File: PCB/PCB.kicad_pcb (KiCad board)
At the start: 2 copper layers, 22 parts, among them J1 12V_IN, J10 Retorno_1, J11 Modulo_Relays, J12 Motor, J13 Retorno_2, J2 5V_OUT, J3 DHT11, J4 Buzzer, J5 Tx, J6 Humidificador, J7 Cooler, J8 Nucleo, J9 9V_OUT, U1 LM7805_TO220, U2 LM7809_TO220

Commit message: Actualizacion de PCB y esquematico
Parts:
- added C7: 10uF, Capacitor_THT:CP_Radial_D4.0mm_P2.00mm, F.Cu at (116.5, 70.0)
- added C8: 0.1uF, Capacitor_THT:C_Disc_D3.0mm_W1.6mm_P2.50mm, F.Cu at (116.2, 74.0)
- added H1: MountingHole_4.3mm_M4_ISO14580_Pad_TopBottom, MountingHole:MountingHole_4.3mm_M4_ISO14580_Pad_TopBottom, F.Cu at (67.5, 60.0)
- added H2: MountingHole_4.3mm_M4_ISO14580_Pad_TopBottom, MountingHole:MountingHole_4.3mm_M4_ISO14580_Pad_TopBottom, F.Cu at (67.5, 99.0)
- added H2: MountingHole_4.3mm_M4_ISO14580_Pad_TopBottom, MountingHole:MountingHole_4.3mm_M4_ISO14580_Pad_TopBottom, F.Cu at (129.7, 99.0)
- added H2: MountingHole_4.3mm_M4_ISO14580_Pad_TopBottom, MountingHole:MountingHole_4.3mm_M4_ISO14580_Pad_TopBottom, F.Cu at (129.7, 60.9)
- added J14: 3_3V_OUT, TerminalBlock_Phoenix:TerminalBlock_Phoenix_MKDS-1,5-2-5.08_1x02_P5.08mm_Horizontal, F.Cu at (115.0, 61.7)
- added U3: LD1117V33, Package_TO_SOT_THT:TO-220-3_Vertical, F.Cu at (116.0, 80.0)
- J5: footprint Connector_Molex:Molex_KK-254_AE-6410-02A_1x02_P2.54mm_Vertical -> Connector_Molex:Molex_KK-254_AE-6410-03A_1x03_P2.54mm_Vertical
- J8: footprint Connector_Molex:Molex_KK-254_AE-6410-08A_1x08_P2.54mm_Vertical -> Connector_Molex:Molex_KK-254_AE-6410-09A_1x09_P2.54mm_Vertical
- moved J13 85.9 mm to (129.0, 89.0), turned to 90 degrees
- moved J3 84.4 mm to (95.5, 100.5), turned to 180 degrees
- moved J10 75.5 mm to (115.0, 98.7), turned to 0 degrees
- moved J6 73.7 mm to (109.3, 100.5), turned to 180 degrees
- moved J8 73.1 mm to (66.5, 87.2), turned to 90 degrees
- moved J2 71.3 mm to (106.8, 61.2), turned to 180 degrees
- moved J1 69.4 mm to (92.0, 61.1), turned to 180 degrees
- moved U1 68.2 mm to (98.4, 78.5), turned to -90 degrees
- moved C3 67.8 mm to (105.2, 70.0), turned to 180 degrees
- moved J4 67.3 mm to (86.3, 100.5), turned to 180 degrees
- moved C4 65.7 mm to (105.5, 74.5), turned to 180 degrees
- moved C2 63.7 mm to (92.0, 75.3)
- moved C1 63.7 mm to (88.0, 75.5)
- moved J12 63.3 mm to (129.0, 77.5), turned to 90 degrees
- moved J7 62.1 mm to (102.3, 100.5), turned to 180 degrees
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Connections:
- J10 pad 2: unconnected-(J10-Pin_2-Pad2) -> B15_R
- J11 pad 2: +12V -> +5V
- J11 pad 6: +5V -> Pin_Motor
- J13 pad 1: +12V_R -> unconnected-(J13-Pin_1-Pad1)
- J13 pad 2: B15_R -> +12V_R
- J8 pad 1: PIN_LAMPARA -> A11
- J8 pad 2: B15 -> B12
- J8 pad 3: B13 -> A9
- J8 pad 4: A11 -> B15
- J8 pad 5: B12 -> B13
- J8 pad 6: A9 -> PIN_LAMPARA
- J8 pad 7: +9V -> Pin_Motor
- J8 pad 8: GND -> +9V
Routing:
- net GND: track 30.2 -> 288.4 mm
- net +3_3V: track 0.00 -> 135.4 mm
- net Net-(D1-K): track 0.00 -> 100.9 mm
- net +5V: track 0.00 -> 58.3 mm
- net A9: track 0.00 -> 35.0 mm
- net +9V: track 0.00 -> 34.6 mm
- net Pin_Motor: track 0.00 -> 31.3 mm
- net PIN_LAMPARA: track 0.00 -> 30.1 mm
- net B13: track 0.00 -> 29.3 mm
- net B15: track 0.00 -> 28.5 mm
- net B12: track 0.00 -> 27.3 mm
- net B15_R: track 0.00 -> 21.3 mm
- net A11: track 0.00 -> 20.3 mm
- net +12V_R: track 29.0 -> 10.8 mm
- net B13_R: track 0.00 -> 6.44 mm
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
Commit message: Actualizacion del PCB
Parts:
- added J15: Encoder_Rotativo, Connector_Molex:Molex_KK-254_AE-6410-05A_1x05_P2.54mm_Vertical, F.Cu at (155.5, 93.4)
- added J16: Encoder_Motor, Connector_Molex:Molex_KK-254_AE-6410-03A_1x03_P2.54mm_Vertical, F.Cu at (146.0, 96.0)
- added J17: LCD, Connector_Molex:Molex_KK-254_AE-6410-04A_1x04_P2.54mm_Vertical, F.Cu at (165.0, 102.3)
- J11: value Modulo_Relays -> Modulo_Reles
- J8: footprint Connector_Molex:Molex_KK-254_AE-6410-09A_1x09_P2.54mm_Vertical -> Connector_Molex:Molex_KK-254_AE-6410-15A_1x15_P2.54mm_Vertical
- moved J9 59.3 mm to (133.0, 73.2), turned to 180 degrees
- moved J14 56.3 mm to (170.0, 73.2), turned to 180 degrees
- moved J8 55.5 mm to (116.0, 112.4)
- moved D1 54.4 mm to (136.3, 82.0)
- moved J1 54.3 mm to (145.0, 73.2)
- moved C7 54.1 mm to (169.5, 80.9), turned to -90 degrees
- moved H4 53.7 mm to (179.5, 119.0)
- moved C3 53.6 mm to (157.5, 82.0)
- moved C4 53.6 mm to (157.8, 86.5)
- moved U3 53.1 mm to (168.5, 88.0)
- moved H3 52.9 mm to (116.5, 119.0)
- moved U1 51.9 mm to (150.2, 82.5)
- moved J2 51.7 mm to (157.0, 73.2)
- moved J4 51.5 mm to (135.2, 116.5)
- moved J6 51.5 mm to (158.2, 116.5)
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- renumbered H2 to H3, H2 to H4
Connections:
- J11 pad 3: B15 -> PIN_MOTOR
- J11 pad 4: B13 -> PIN_LAMPARA
- J11 pad 5: PIN_LAMPARA -> B13
- J11 pad 6: Pin_Motor -> B15
- J14 pad 1: +3_3V -> GND
- J14 pad 2: GND -> +3_3V
- J8 pad 4: B15 -> SCL
- J8 pad 5: B13 -> SDA
- J8 pad 6: PIN_LAMPARA -> CLK
- J8 pad 7: Pin_Motor -> DT
- J8 pad 8: +9V -> SW
- J8 pad 9: GND -> PIN_ENCODER
- J9 pad 1: +9V -> GND
- J9 pad 2: GND -> +9V
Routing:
- net +5V: track 58.3 -> 119.4 mm
- net SDA: track 0.00 -> 57.2 mm
- net SCL: track 0.00 -> 54.9 mm
- net SW: track 0.00 -> 45.2 mm
- net CLK: track 0.00 -> 44.7 mm
- net DT: track 0.00 -> 44.4 mm
- net PIN_ENCODER: track 0.00 -> 33.7 mm
- net Pin_Motor: track 31.3 -> 0.00 mm
- net PIN_MOTOR: track 0.00 -> 26.1 mm
- net Net-(D1-K): track 100.9 -> 84.3 mm
- net B15: track 28.5 -> 12.1 mm
- net GND: track 288.4 -> 301.1 mm
- net B13: track 29.3 -> 17.4 mm
- net +3_3V: track 135.4 -> 146.1 mm
- net PIN_LAMPARA: track 30.1 -> 21.1 mm
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- added copper zone on B.Cu, net GND
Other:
- board outline added: 71.5 x 56 mm

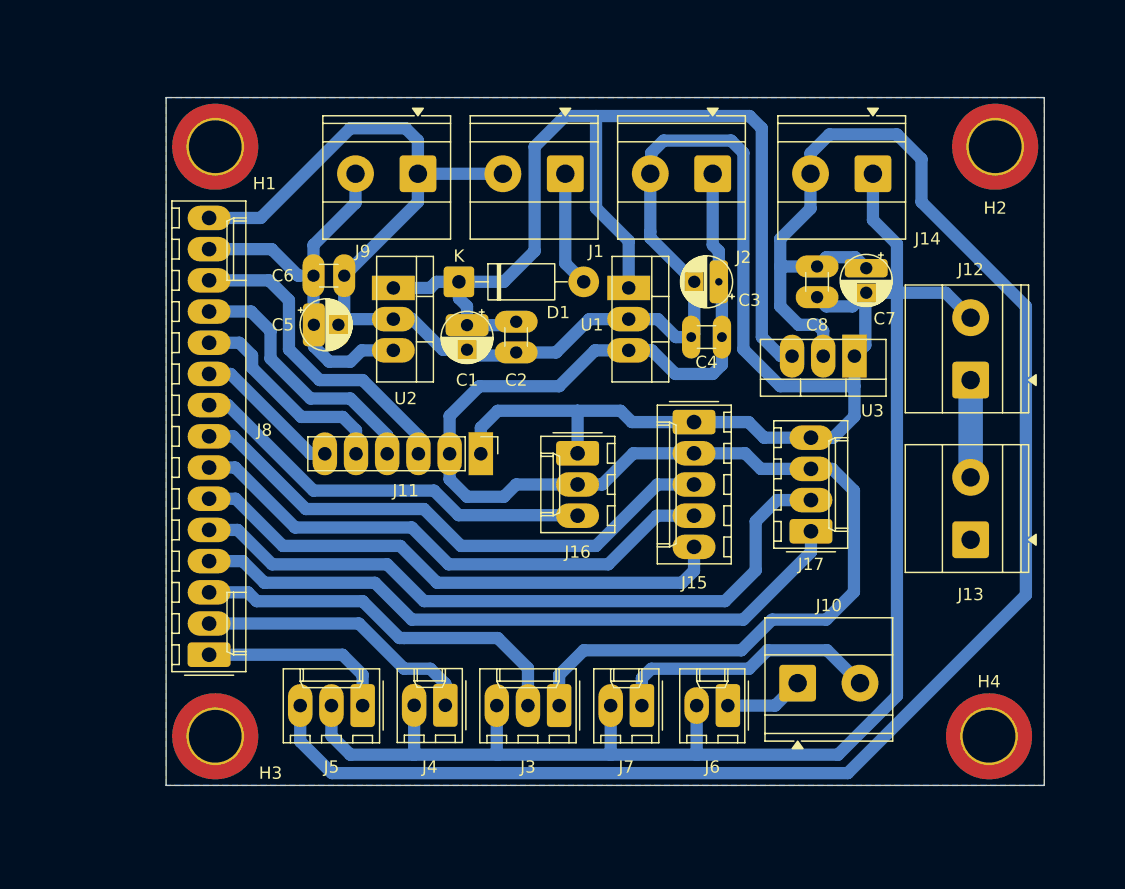
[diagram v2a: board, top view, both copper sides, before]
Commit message: Actualizacion del modelo 3D
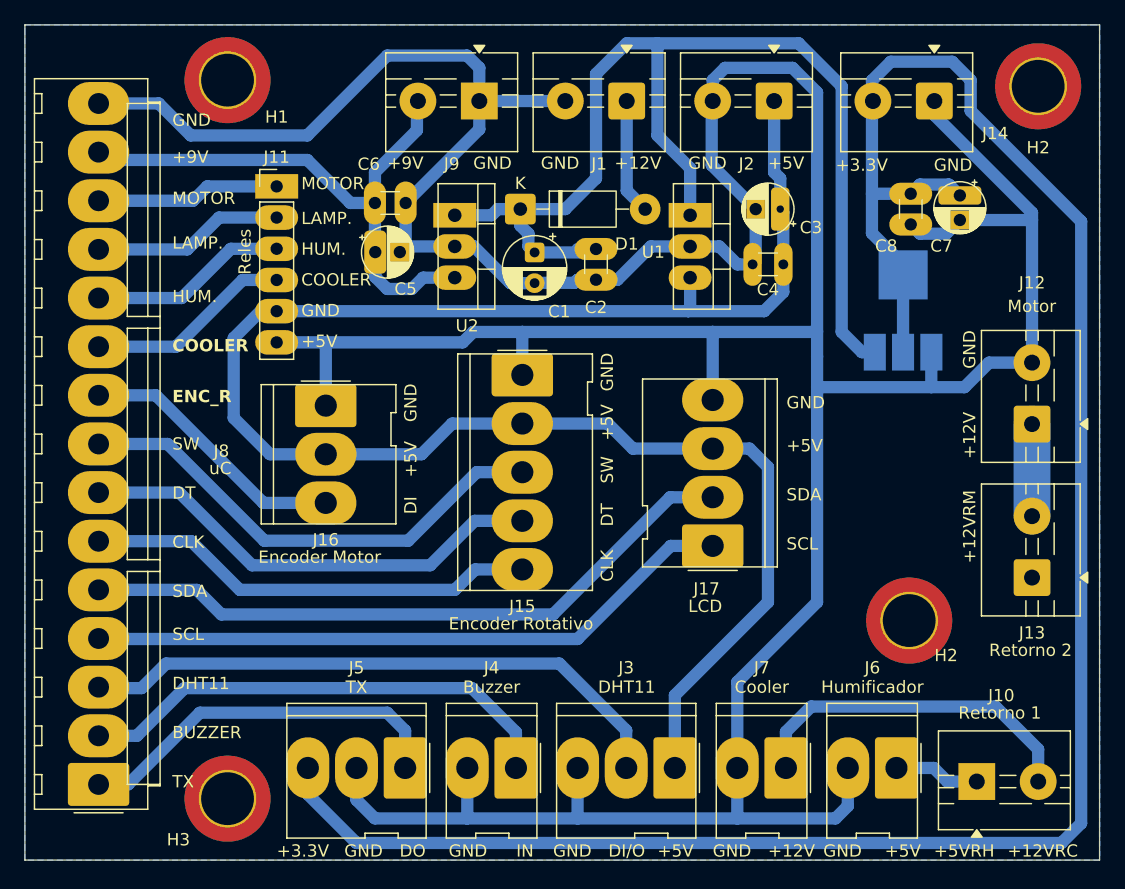
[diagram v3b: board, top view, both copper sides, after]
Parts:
- removed H4: MountingHole_4.3mm_M4_ISO14580_Pad_TopBottom, MountingHole:MountingHole_4.3mm_M4_ISO14580_Pad_TopBottom
- added H2: MountingHole_4.3mm_M4_ISO14580_Pad_TopBottom, MountingHole:MountingHole_4.3mm_M4_ISO14580_Pad_TopBottom, F.Cu at (183.5, 66.1)
- C1: value 0.22uF -> 0.33uF; footprint Capacitor_THT:CP_Radial_D4.0mm_P2.00mm -> Capacitor_THT:CP_Radial_D5.0mm_P2.50mm
- J1, J10, J12, J13, J14, J2, J9: footprint TerminalBlock_Phoenix:TerminalBlock_Phoenix_MKDS-1,5-2-5.08_1x02_P5.08mm_Horizontal -> TerminalBlock:TerminalBlock_MaiXu_MX126-5.0-02P_1x02_P5.00mm
- J15: footprint Connector_Molex:Molex_KK-254_AE-6410-05A_1x05_P2.54mm_Vertical -> Connector_Molex:Molex_KK-396_5273-05A_1x05_P3.96mm_Vertical
- J16, J3: footprint Connector_Molex:Molex_KK-254_AE-6410-03A_1x03_P2.54mm_Vertical -> Connector_Molex:Molex_KK-396_5273-03A_1x03_P3.96mm_Vertical
- J17: footprint Connector_Molex:Molex_KK-254_AE-6410-04A_1x04_P2.54mm_Vertical -> Connector_Molex:Molex_KK-396_5273-04A_1x04_P3.96mm_Vertical
- J4, J7: footprint Connector_Molex:Molex_KK-254_AE-6410-02A_1x02_P2.54mm_Vertical -> Connector_Molex:Molex_KK-396_5273-02A_1x02_P3.96mm_Vertical
- J5: value Tx -> TX; footprint Connector_Molex:Molex_KK-254_AE-6410-03A_1x03_P2.54mm_Vertical -> Connector_Molex:Molex_KK-396_5273-03A_1x03_P3.96mm_Vertical
- J6: value Humidificador -> Humidi.; footprint Connector_Molex:Molex_KK-254_AE-6410-02A_1x02_P2.54mm_Vertical -> Connector_Molex:Molex_KK-396_5273-02A_1x02_P3.96mm_Vertical
- J8: footprint Connector_Molex:Molex_KK-254_AE-6410-15A_1x15_P2.54mm_Vertical -> Connector_Molex:Molex_KK-396_A-41791-0015_1x15_P3.96mm_Vertical
- U3: footprint Package_TO_SOT_THT:TO-220-3_Vertical -> Package_TO_SOT_SMD:SOT-223; moved to B.Cu
- moved H2 39.2 mm to (173.0, 109.6)
- moved J11 27.4 mm to (121.5, 74.2), turned to 0 degrees
- moved J16 20.9 mm to (125.5, 92.1)
- moved J10 16.6 mm to (178.5, 122.7)
- moved J6 14.6 mm to (172.0, 121.6)
- moved J15 14.5 mm to (141.5, 89.6)
- moved J8 13.9 mm to (107.0, 122.9)
- moved J7 12.8 mm to (163.0, 121.6)
- moved J3 10.7 mm to (153.9, 121.6)
- moved C7 9.65 mm to (177.1, 75.0)
- moved C8 9.65 mm to (173.1, 74.8)
- moved C2 8.79 mm to (147.5, 79.3)
- moved J17 8.09 mm to (157.0, 103.5)
- moved C1 8.08 mm to (142.5, 79.6)
- moved C3 7.75 mm to (162.5, 76.1)
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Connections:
- net +12V_R renamed +12V_R_Motor
- net B13_R renamed +5V_R_Humidificador
- net B15_R renamed +12V_R_Cooler
- H1 pad 1: (no net) -> GND
- H2 pad 1: (no net) -> GND
- H3 pad 1: (no net) -> GND
- J11 pad 1: GND -> PIN_MOTOR
- J11 pad 2: +5V -> PIN_LAMPARA
- J11 pad 3: PIN_MOTOR -> B13
- J11 pad 4: PIN_LAMPARA -> B15
- J11 pad 5: B13 -> +5V
- J11 pad 6: B15 -> GND
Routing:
- net GND: track 301.1 -> 349.5 mm
- net +5V: track 119.4 -> 146.3 mm
- net +3_3V: track 146.1 -> 171.9 mm
- net A9: track 31.6 -> 49.1 mm
- net B12: track 23.0 -> 40.5 mm
- net A11: track 15.7 -> 31.0 mm
- net +9V: track 32.2 -> 47.2 mm
- net PIN_ENCODER: track 33.7 -> 22.1 mm
- net PIN_MOTOR: track 26.1 -> 15.0 mm
- net Net-(D1-K): track 84.3 -> 92.8 mm
- net CLK: track 44.7 -> 36.8 mm
- net +12V_R_Cooler: track 22.0 -> 28.4 mm
- net DT: track 44.4 -> 38.5 mm
- net PIN_LAMPARA: track 21.1 -> 15.6 mm
- net SW: track 45.2 -> 40.1 mm
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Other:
- board size 71.5 x 56 mm -> 87.5 x 68 mm
- board text added: "+12V"
- board text added: "+12VRC"
- board text added: "+12VRM"
- board text added: "+3.3V"
- board text added: "+5V"
- board text added: "+5VRH"
- board text added: "+9V"
- board text added: "BUZZER"
- board text added: "Buzzer"
- board text added: "CLK"
- board text added: "COOLER"
- board text added: "Cooler"
- board text added: "DHT11"
- board text added: "DI"
- board text added: "DI/O"
- board text added: "DO"
- board text added: "DT"
- board text added: "ENC_R"
- board text added: "Encoder Motor"
- board text added: "Encoder Rotativo"
- board text added: "GND"
- board text added: "HUM."
- board text added: "Humificador"
- board text added: "IN"
- board text added: "LAMP."
- board text added: "LCD"
- board text added: "MOTOR"
- board text added: "Motor"
- board text added: "Reles"
- board text added: "Retorno 1"
- board text added: "Retorno 2"
- board text added: "SCL"
- board text added: "SDA"
- board text added: "SW"
- board text added: "TX"
- board text added: "uC"
